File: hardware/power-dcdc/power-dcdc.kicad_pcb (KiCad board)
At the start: 2 copper layers, 120 x 90 mm, 69 parts, among them J1 SOLAR_IN, J2 DCDC-MEASURES, J3 DCDC-PWM, J4 BATT2, J5 BATT1, Q1 SIR164ADP, Q2 SIR164ADP, Q3 SI7149ADP, Q4 SI7149ADP, Q5 SI7149ADP, Q6 SI7149ADP, U1 LP4951C, U2 NCP5901B, U3 PAC1953-1, U4 DGD0215, U5 DGD0215

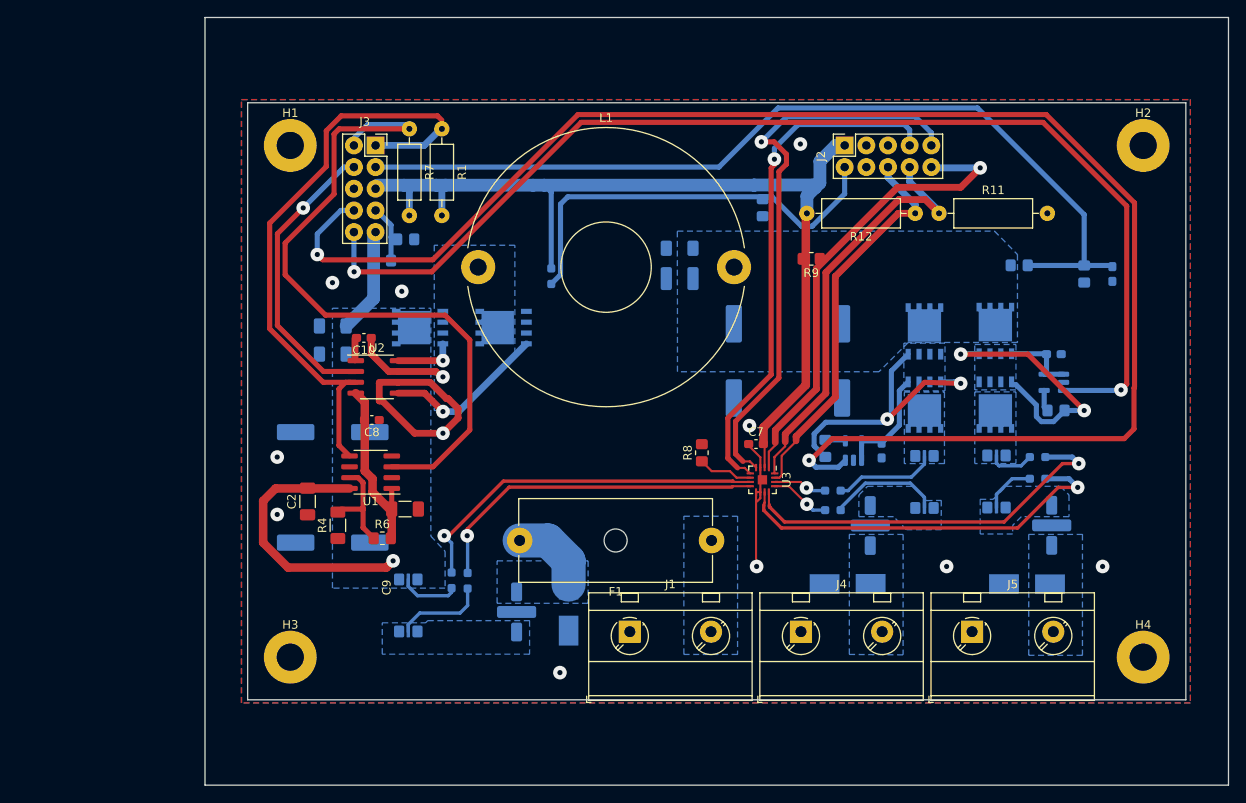
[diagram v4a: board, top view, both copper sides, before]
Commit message: Import schematic changes to PCB; re-route the output path.
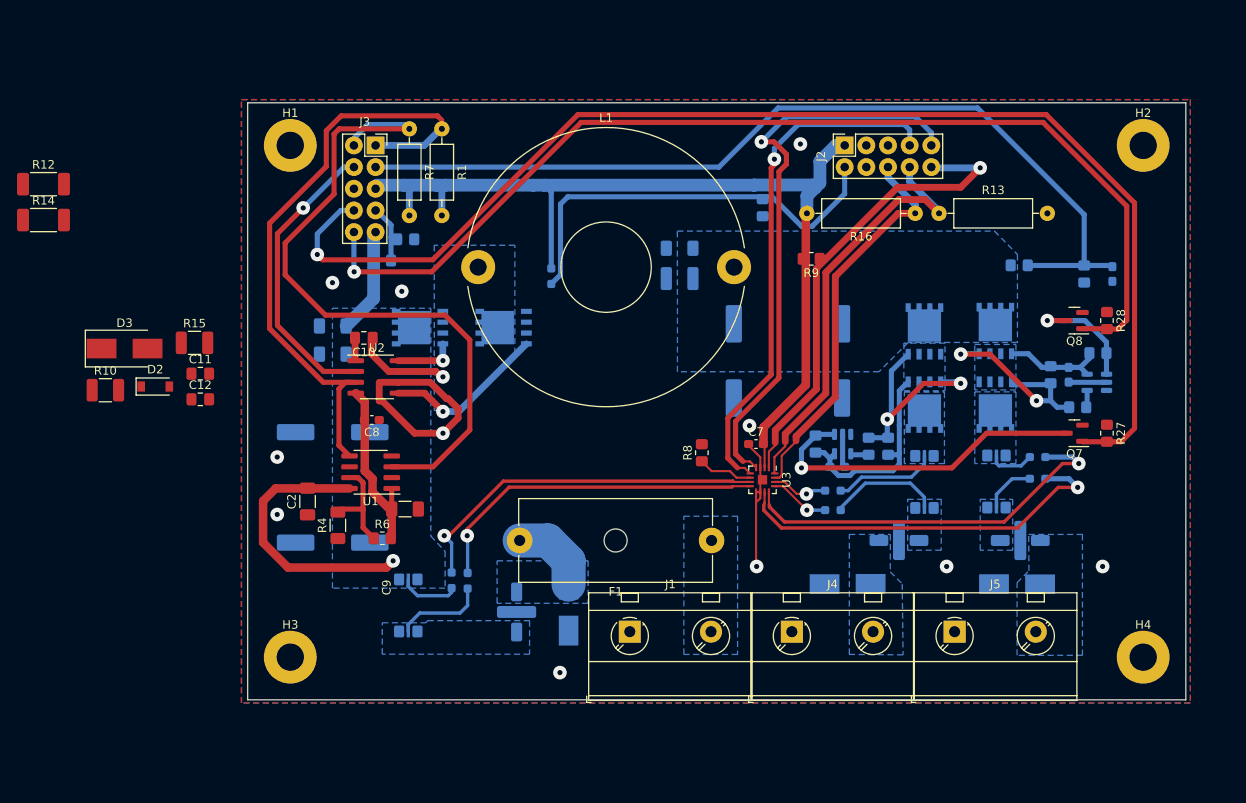
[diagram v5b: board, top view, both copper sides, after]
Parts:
- added C11: N/A, Capacitor_SMD:C_0805_2012Metric_Pad1.18x1.45mm_HandSolder, F.Cu at (44.5, 111.8)
- added C12: N/A, Capacitor_SMD:C_0805_2012Metric_Pad1.18x1.45mm_HandSolder, F.Cu at (44.5, 114.8)
- added D2: PMEG4005, Diode_SMD:D_SOD-123, F.Cu at (39.2, 113.3)
- added D3: SMBJ16A, Diode_SMD:D_SMB_Handsoldering, F.Cu at (35.6, 108.8)
- added Q7: BSS123, Package_TO_SOT_SMD:SOT-23, F.Cu at (146.9, 118.7)
- added Q8: BSS123, Package_TO_SOT_SMD:SOT-23, F.Cu at (146.9, 105.5)
- added R10: 0, Resistor_SMD:R_1210_3225Metric_Pad1.30x2.65mm_HandSolder, F.Cu at (33.3, 113.7)
- added R12: 0.02, Resistor_SMD:R_2010_5025Metric_Pad1.40x2.65mm_HandSolder, F.Cu at (26.1, 89.5)
- added R14: 0.02, Resistor_SMD:R_2010_5025Metric_Pad1.40x2.65mm_HandSolder, F.Cu at (26.1, 93.8)
- added R15: N/A, Resistor_SMD:R_1210_3225Metric_Pad1.30x2.65mm_HandSolder, F.Cu at (43.8, 108.2)
- added R21: 47k, Resistor_SMD:R_0805_2012Metric_Pad1.20x1.40mm_HandSolder, B.Cu at (116.6, 120.0)
- added R22: 47k, Resistor_SMD:R_0805_2012Metric_Pad1.20x1.40mm_HandSolder, B.Cu at (149.7, 109.3)
- added R23: 100k, Resistor_SMD:R_0805_2012Metric_Pad1.20x1.40mm_HandSolder, B.Cu at (125.1, 120.3)
- added R24: 100k, Resistor_SMD:R_0805_2012Metric_Pad1.20x1.40mm_HandSolder, B.Cu at (144.1, 111.9)
- added R27: 100k, Resistor_SMD:R_0805_2012Metric_Pad1.20x1.40mm_HandSolder, F.Cu at (150.7, 118.7)
- added R28: 100k, Resistor_SMD:R_0805_2012Metric_Pad1.20x1.40mm_HandSolder, F.Cu at (150.7, 105.5)
- C10: value 100nF -> 1µF; footprint Capacitor_SMD:C_0603_1608Metric_Pad1.08x0.95mm_HandSolder -> Capacitor_SMD:C_0805_2012Metric_Pad1.18x1.45mm_HandSolder
- Q1, Q2: value SIR164ADP -> SIR186LDP
- moved C17 5.54 mm to (119.1, 122.7), turned to 180 degrees
- moved R19 5.09 mm to (122.8, 120.3), turned to -90 degrees
- moved U5 5.04 mm to (149.6, 112.8)
- moved C20 4.09 mm to (140.6, 131.3), turned to 180 degrees
- moved C19 3.79 mm to (126.4, 131.3), turned to 0 degrees
- moved C18 2.97 mm to (146.3, 111.9), turned to 90 degrees
- moved R20 2.57 mm to (147.3, 115.7), turned to 0 degrees
- moved J5 2.05 mm to (132.9, 142.0)
- moved U4 1.48 mm to (119.8, 120.0), turned to -90 degrees
- moved D5 1.17 mm to (140.2, 136.4)
- moved J4 1.07 mm to (113.8, 142.0)
- renumbered C11 to C13, C12 to C14, C13 to C15, C14 to C16, C15 to C19, C16 to C20, C19 to C21, D2 to D4, D3 to D5, R10 to R11, R11 to R13, R12 to R16, R13 to R17, R14 to R18, R15 to R19, R16 to R20, R17 to R25, R18 to R26
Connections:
- C17 pad 1: Net-(C17-Pad1) -> GND
- C17 pad 2: GND -> Net-(C17-Pad2)
- C18 pad 1: Net-(C18-Pad1) -> GND
- C18 pad 2: GND -> Net-(C18-Pad2)
- Q2 pad 5: Net-(C10-Pad1) -> Net-(Q2-Pad5)
- Q3 pad 1: Net-(C17-Pad1) -> Net-(C17-Pad2)
- Q3 pad 2: Net-(C17-Pad1) -> Net-(C17-Pad2)
- Q3 pad 3: Net-(C17-Pad1) -> Net-(C17-Pad2)
- Q4 pad 1: Net-(C18-Pad1) -> Net-(C18-Pad2)
- Q4 pad 2: Net-(C18-Pad1) -> Net-(C18-Pad2)
- Q4 pad 3: Net-(C18-Pad1) -> Net-(C18-Pad2)
- Q5 pad 1: Net-(C17-Pad1) -> Net-(C17-Pad2)
- Q5 pad 2: Net-(C17-Pad1) -> Net-(C17-Pad2)
- Q5 pad 3: Net-(C17-Pad1) -> Net-(C17-Pad2)
- Q6 pad 1: Net-(C18-Pad1) -> Net-(C18-Pad2)
- Q6 pad 2: Net-(C18-Pad1) -> Net-(C18-Pad2)
- Q6 pad 3: Net-(C18-Pad1) -> Net-(C18-Pad2)
- U2 pad 1: Net-(C10-Pad2) -> Net-(D2-Pad2)
- U4 pad 1: Net-(C17-Pad1) -> Net-(Q7-Pad3)
- U4 pad 3: BATT2_ON -> GND
- U4 pad 5: Net-(C17-Pad1) -> Net-(C17-Pad2)
- U5 pad 1: Net-(C18-Pad1) -> Net-(Q8-Pad3)
- U5 pad 3: BATT1_ON -> GND
- U5 pad 5: Net-(C18-Pad1) -> Net-(C18-Pad2)
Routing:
- net Net-(Q7-Pad3): track 0.00 -> 39.5 mm, vias 0 -> 1
- net BATT2_ON: track 186.3 -> 148.5 mm, vias 2 -> 1
- net Net-(C17-Pad2): track 0.00 -> 24.3 mm
- net Net-(Q8-Pad3): track 0.00 -> 14.0 mm, vias 0 -> 1
- net Net-(C17-Pad1): track 13.2 -> 0.00 mm
- net Net-(C18-Pad2): track 0.00 -> 12.1 mm
- net BATT1_ON: track 135.2 -> 125.6 mm, vias 2 -> 1
- net Net-(C18-Pad1): track 8.78 -> 0.00 mm
- net GND: track 41.6 -> 50.0 mm
- net Net-(Q3-Pad4): track 33.9 -> 26.4 mm
- net Net-(Q4-Pad4): track 31.0 -> 24.2 mm
- net Net-(D2-Pad2): track 0.00 -> 2.58 mm
- net Net-(C10-Pad2): track 2.58 -> 0.00 mm
- net Net-(R19-Pad2): track 2.40 -> 1.73 mm
- added copper zone on B.Cu, net Net-(C17-Pad2)
- added copper zone on B.Cu, net Net-(C18-Pad2)
- removed copper zone on B.Cu, net Net-(C17-Pad1)
- removed copper zone on B.Cu, net Net-(C18-Pad1)
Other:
- board size 120 x 90 mm -> 110 x 70 mm

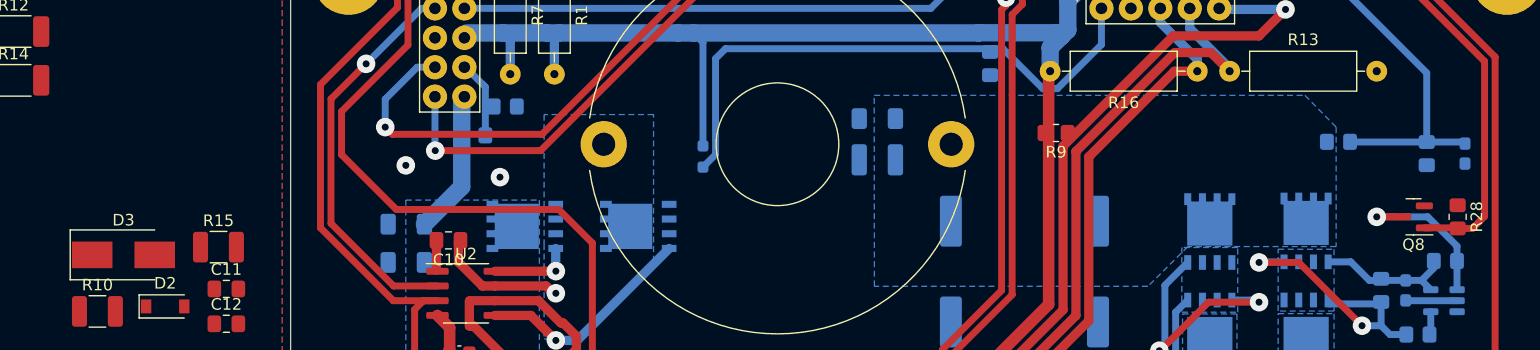
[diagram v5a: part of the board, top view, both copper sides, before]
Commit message: PCB: Add the TVS diode at the output of the DC/DC
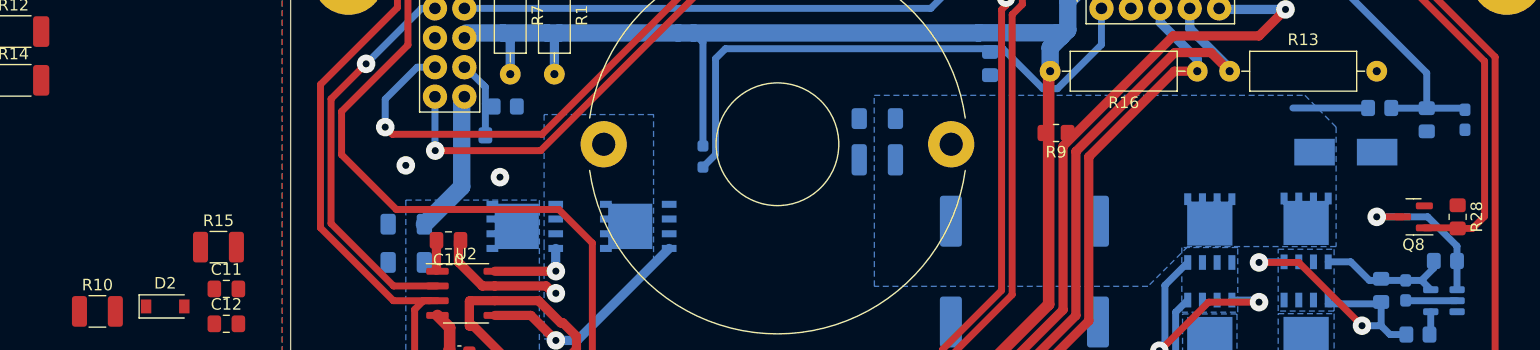
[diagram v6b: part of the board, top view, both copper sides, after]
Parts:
- D3: moved to B.Cu
- moved D3 105.9 mm to (141.1, 99.9)
- moved R25 4.60 mm to (144.0, 96.1)
- moved C21 2.92 mm to (151.4, 97.2)
- moved R26 2.92 mm to (148.1, 97.2)
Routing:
- net Net-(C13-Pad1): track 0.00 -> 6.49 mm
- net PWM_V: track 107.0 -> 100.5 mm
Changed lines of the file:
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@@
-    )
-  )
-  (footprint "Diode_SMD:D_SMB_Handsoldering" (layer "F.Cu")
-    (at 35.57 108.82)
-    (descr "Diode SMB (DO-214AA) Handsoldering")
-    (tags "Diode SMB (DO-214AA) Handsoldering")
-    (property "P/N" " SMBJ16Ae3/TR13 (M)")
-    (property "Sheetfile" "power-dcdc.kicad_sch")
-    (property "Sheetname" "")
-    (attr smd)
-    (fp_text reference "D3" (at 0 -3) (layer "F.SilkS")
-      (effects (font (size 1 1) (thickness 0.15)))
-    )
-    (fp_text value "SMBJ16A" (at 0 3) (layer "F.Fab")
-      (effects (font (size 1 1) (thickness 0.15)))
-    )
-    (fp_text user "${REFERENCE}" (at 0 -3) (layer "F.Fab")
-      (effects (font (size 1 1) (thickness 0.15)))
-    )
-    (fp_line (start -4.6 -2.15) (end -4.6 2.15) (layer "F.SilkS") (width 0.12))
-    (fp_line (start -4.6 2.15) (end 2.7 2.15) (layer "F.SilkS") (width 0.12))
-    (fp_line (start -4.6 -2.15) (end 2.7 -2.15) (layer "F.SilkS") (width 0.12))
-    (fp_line (start 4.7 -2.25) (end 4.7 2.25) (layer "F.CrtYd") (width 0.05))
-    (fp_line (start 4.7 2.25) (end -4.7 2.25) (layer "F.CrtYd") (width 0.05))
-    (fp_line (start -4.7 2.25) (end -4.7 -2.25) (layer "F.CrtYd") (width 0.05))
-    (fp_line (start -4.7 -2.25) (end 4.7 -2.25) (layer "F.CrtYd") (width 0.05))
-    (fp_line (start -0.64944 0.00102) (end -1.55114 0.00102) (layer "F.Fab") (width 0.1))
-    (fp_line (start -0.64944 0.00102) (end 0.50118 -0.79908) (layer "F.Fab") (width 0.1))
-    (fp_line (start 0.50118 0.75032) (end 0.50118 -0.79908) (layer "F.Fab") (width 0.1))
-    (fp_line (start 2.3 -2) (end -2.3 -2) (layer "F.Fab") (width 0.1))
-    (fp_line (start 2.3 -2) (end 2.3 2) (layer "F.Fab") (width 0.1))
-    (fp_line (start 2.3 2) (end -2.3 2) (layer "F.Fab") (width 0.1))
-    (fp_line (start -0.64944 0.00102) (end 0.50118 0.75032) (layer "F.Fab") (width 0.1))
-    (fp_line (start -0.64944 -0.79908) (end -0.64944 0.80112) (layer "F.Fab") (width 0.1))
-    (fp_line (start -2.3 2) (end -2.3 -2) (layer "F.Fab") (width 0.1))
-    (fp_line (start 0.50118 0.00102) (end 1.4994 0.00102) (layer "F.Fab") (width 0.1))
-    (pad "1" smd rect (at -2.7 0) (size 3.5 2.3) (layers "F.Cu" "F.Paste" "F.Mask")
-      (net 8 "Net-(C13-Pad1)") (pinfunction "A1") (pintype "passive"))
-    (pad "2" smd rect (at 2.7 0) (size 3.5 2.3) (layers "F.Cu" "F.Paste" "F.Mask")
-      (net 2 "GND") (pinfunction "A2") (pintype "passive"))
-    (model "${KICAD6_3DMODEL_DIR}/Diode_SMD.3dshapes/D_SMB.wrl"
-      (offset (xyz 0 0 0))
-      (scale (xyz 1 1 1))
-      (rotate (xyz 0 0 0))
     )
   )
@@
   )
   (footprint "Resistor_SMD:R_0805_2012Metric_Pad1.20x1.40mm_HandSolder" (layer "B.Cu")
-    (at 148.082 100.076 -90)
+    (at 148.082 97.155 -90)
     (descr "Resistor SMD 0805 (2012 Metric), square (rectangular) end terminal, IPC_7351 nominal with elongated pad for handsoldering. (Body size source: IPC-SM-782 page 72, https://www.pcb-3d.com/wordpress/wp-content/uploads/ipc-sm-782a_amendment_1_and_2.pdf), generated with kicad-footprint-generator")
     (tags "resistor handsolder")
@@
     )
   )
+  (footprint "Diode_SMD:D_SMB_Handsoldering" (layer "B.Cu")
+    (at 141.097 99.949)
+    (descr "Diode SMB (DO-214AA) Handsoldering")
+    (tags "Diode SMB (DO-214AA) Handsoldering")
+    (property "P/N" " SMBJ16Ae3/TR13 (M)")
+    (property "Sheetfile" "power-dcdc.kicad_sch")
+    (property "Sheetname" "")
+    (attr smd)
+    (fp_text reference "D3" (at 0 3) (layer "B.SilkS")
+      (effects (font (size 1 1) (thickness 0.15)) (justify mirror))
+    )
+    (fp_text value "SMBJ16A" (at 0 -3) (layer "B.Fab")
+      (effects (font (size 1 1) (thickness 0.15)) (justify mirror))
+    )
+    (fp_text user "${REFERENCE}" (at 0 3) (layer "B.Fab")
+      (effects (font (size 1 1) (thickness 0.15)) (justify mirror))
+    )
+    (fp_line (start -4.6 2.15) (end -4.6 -2.15) (layer "B.SilkS") (width 0.12))
+    (fp_line (start -4.6 -2.15) (end 2.7 -2.15) (layer "B.SilkS") (width 0.12))
+    (fp_line (start -4.6 2.15) (end 2.7 2.15) (layer "B.SilkS") (width 0.12))
+    (fp_line (start 4.7 2.25) (end 4.7 -2.25) (layer "B.CrtYd") (width 0.05))
+    (fp_line (start 4.7 -2.25) (end -4.7 -2.25) (layer "B.CrtYd") (width 0.05))
+    (fp_line (start -4.7 -2.25) (end -4.7 2.25) (layer "B.CrtYd") (width 0.05))
+    (fp_line (start -4.7 2.25) (end 4.7 2.25) (layer "B.CrtYd") (width 0.05))
+    (fp_line (start -0.64944 -0.00102) (end -1.55114 -0.00102) (layer "B.Fab") (width 0.1))
+    (fp_line (start -0.64944 -0.00102) (end 0.50118 0.79908) (layer "B.Fab") (width 0.1))
+    (fp_line (start 0.50118 -0.75032) (end 0.50118 0.79908) (layer "B.Fab") (width 0.1))
+    (fp_line (start 2.3 2) (end -2.3 2) (layer "B.Fab") (width 0.1))
+    (fp_line (start 2.3 2) (end 2.3 -2) (layer "B.Fab") (width 0.1))
+    (fp_line (start 2.3 -2) (end -2.3 -2) (layer "B.Fab") (width 0.1))
+    (fp_line (start -0.64944 -0.00102) (end 0.50118 -0.75032) (layer "B.Fab") (width 0.1))
+    (fp_line (start -0.64944 0.79908) (end -0.64944 -0.80112) (layer "B.Fab") (width 0.1))
+    (fp_line (start -2.3 -2) (end -2.3 2) (layer "B.Fab") (width 0.1))
+    (fp_line (start 0.50118 -0.00102) (end 1.4994 -0.00102) (layer "B.Fab") (width 0.1))
+    (pad "1" smd rect (at -2.7 0) (size 3.5 2.3) (layers "B.Cu" "B.Paste" "B.Mask")
+      (net 8 "Net-(C13-Pad1)") (pinfunction "A1") (pintype "passive"))
+    (pad "2" smd rect (at 2.7 0) (size 3.5 2.3) (layers "B.Cu" "B.Paste" "B.Mask")
+      (net 2 "GND") (pinfunction "A2") (pintype "passive"))
+    (model "${KICAD6_3DMODEL_DIR}/Diode_SMD.3dshapes/D_SMB.wrl"
+      (offset (xyz 0 0 0))
+      (scale (xyz 1 1 1))
+      (rotate (xyz 0 0 0))
+    )
+  )
   (footprint "Resistor_SMD:R_0805_2012Metric_Pad1.20x1.40mm_HandSolder" (layer "B.Cu")
-    (at 140.462 99.06)
+    (at 144.018 96.139)
     (descr "Resistor SMD 0805 (2012 Metric), square (rectangular) end terminal, IPC_7351 nominal with elongated pad for handsoldering. (Body size source: IPC-SM-782 page 72, https://www.pcb-3d.com/wordpress/wp-content/uploads/ipc-sm-782a_amendment_1_and_2.pdf), generated with kicad-footprint-generator")
     (tags "resistor handsolder")
@@
   )
   (footprint "Capacitor_SMD:C_0603_1608Metric_Pad1.08x0.95mm_HandSolder" (layer "B.Cu")
-    (at 151.384 100.076 90)
+    (at 151.384 97.155 90)
     (descr "Capacitor SMD 0603 (1608 Metric), square (rectangular) end terminal, IPC_7351 nominal with elongated pad for handsoldering. (Body size source: IPC-SM-782 page 76, https://www.pcb-3d.com/wordpress/wp-content/uploads/ipc-sm-782a_amendment_1_and_2.pdf), generated with kicad-footprint-generator")
     (tags "capacitor handsolder")
@@
   (segment (start 84.7852 89.662) (end 109.37738 89.662) (width 1.5) (layer "B.Cu") (net 5))
   (segment (start 85.598 99.4175) (end 85.598 90.4748) (width 0.6) (layer "B.Cu") (net 5))
+  (segment (start 143.018 96.139) (end 136.525 96.139) (width 0.6) (layer "B.Cu") (net 8))
   (segment (start 67.056 133.7056) (end 66.2686 134.493) (width 1) (layer "F.Cu") (net 9))
   (segment (start 53.2765 125.222) (end 61.946 125.222) (width 1) (layer "F.Cu") (net 9))
@@
   (segment (start 112.194979 80.61) (end 135.5756 80.61) (width 0.6) (layer "B.Cu") (net 18))
   (segment (start 65 87.54) (end 105.264979 87.54) (width 0.6) (layer "B.Cu") (net 18))
-  (segment (start 148.082 99.076) (end 141.478 99.076) (width 0.6) (layer "B.Cu") (net 18))
+  (segment (start 148.082 96.155) (end 145.034 96.155) (width 0.6) (layer "B.Cu") (net 18))
   (segment (start 105.264979 87.54) (end 112.194979 80.61) (width 0.6) (layer "B.Cu") (net 18))
-  (segment (start 148.082 93.1164) (end 148.082 99.076) (width 0.6) (layer "B.Cu") (net 18))
-  (segment (start 148.082 99.076) (end 151.3465 99.076) (width 0.6) (layer "B.Cu") (net 18))
+  (segment (start 148.082 93.1164) (end 148.082 96.155) (width 0.6) (layer "B.Cu") (net 18))
+  (segment (start 145.034 96.155) (end 145.018 96.139) (width 0.6) (layer "B.Cu") (net 18))
+  (segment (start 148.082 96.155) (end 151.3465 96.155) (width 0.6) (layer "B.Cu") (net 18))
   (segment (start 135.5756 80.61) (end 148.082 93.1164) (width 0.6) (layer "B.Cu") (net 18))
   (segment (start 68.834 135.888) (end 68.834 136.652) (width 0.4) (layer "B.Cu") (net 19))
